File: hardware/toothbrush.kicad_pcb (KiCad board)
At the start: 2 copper layers, 41.5 x 19 mm, 16 parts, among them J2 ISP, J3 MOTOR, J4 BATTERY, Q1 FN337N, SW1 button, U1 ATmega328P-A

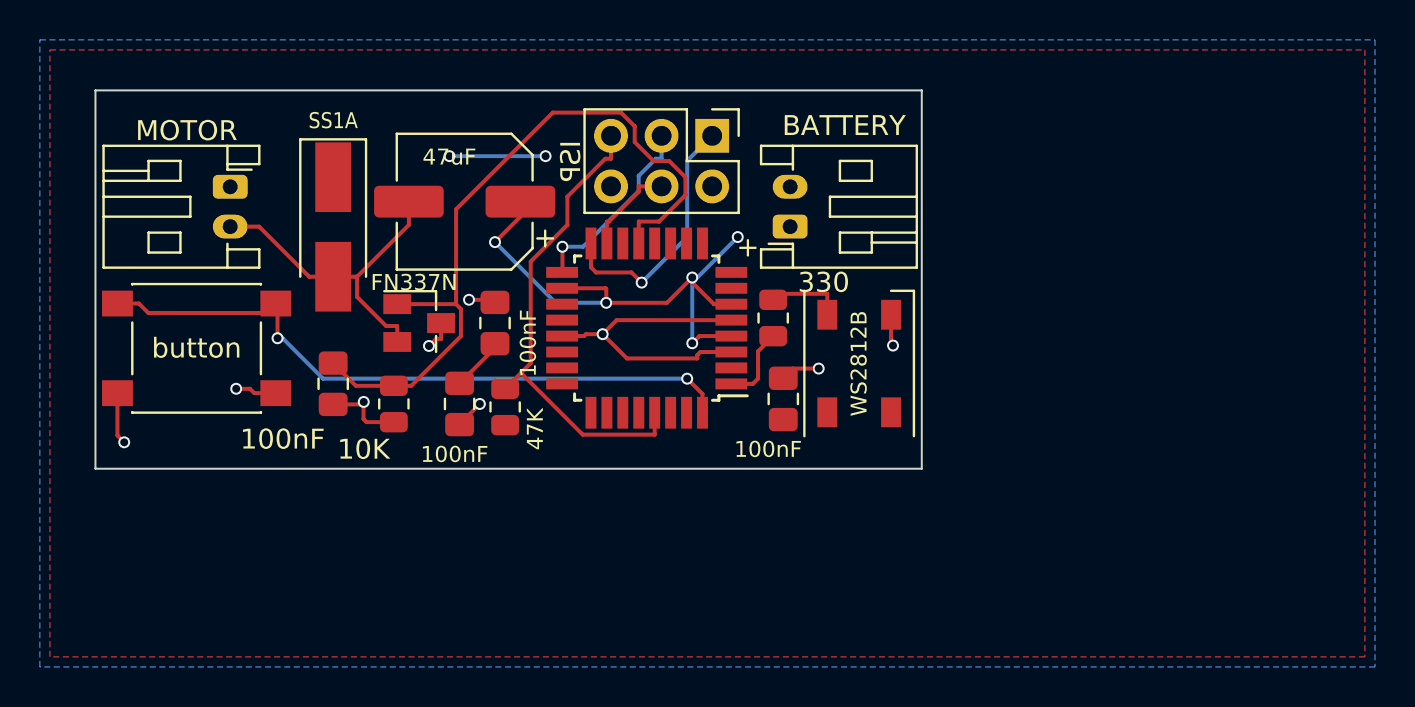
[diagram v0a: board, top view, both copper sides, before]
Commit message: Turn power connector around to be more consistent with other things.
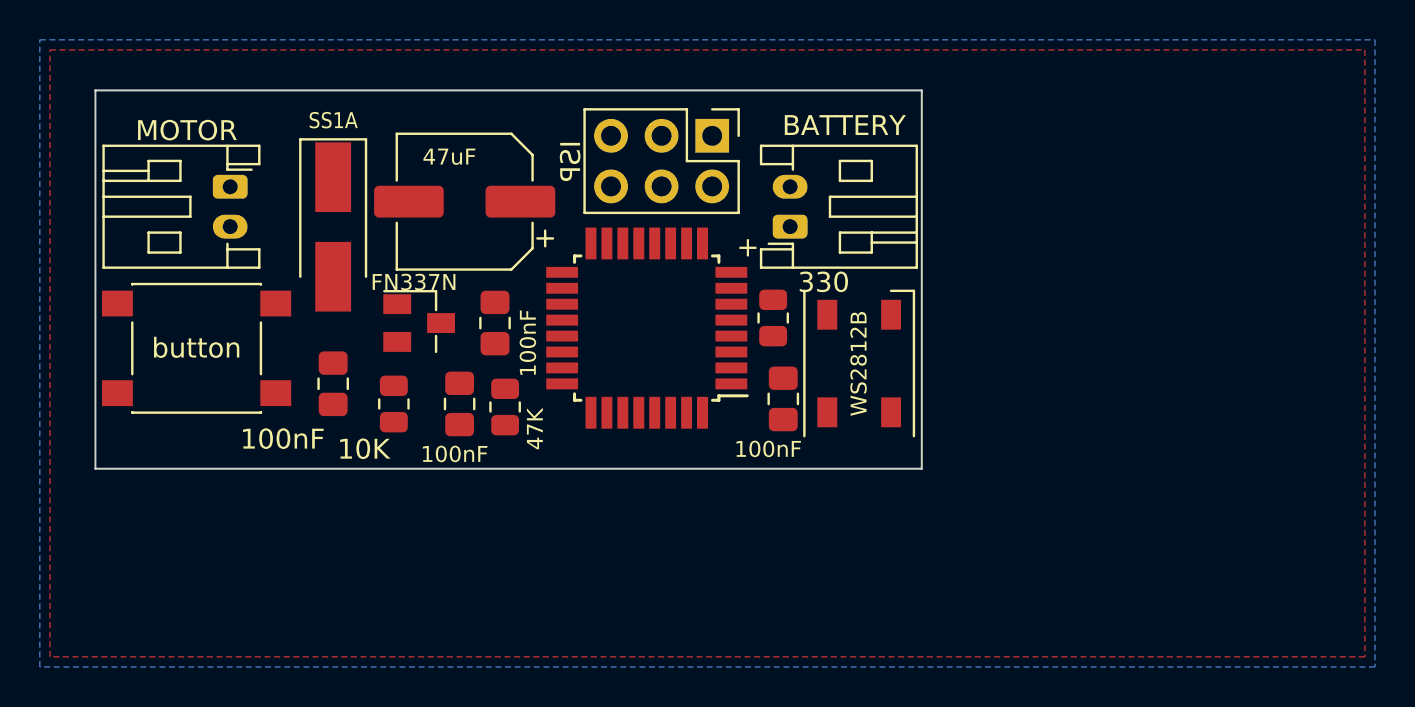
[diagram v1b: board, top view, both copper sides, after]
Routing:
- net /FAN: track 37.6 -> 0.00 mm
- net /VCC: track 35.9 -> 0.00 mm, vias 7 -> 0
- net /BUTTON: track 33.8 -> 0.00 mm, vias 2 -> 0
- net GND: track 32.7 -> 0.00 mm, vias 9 -> 0
- net /RST: track 24.2 -> 0.00 mm
- net Net-(C4-Pad2): track 16.7 -> 0.00 mm
- net /MISO: track 12.9 -> 0.00 mm, vias 1 -> 0
- net /SCK: track 9.70 -> 0.00 mm, vias 1 -> 0
- net /MOSI: track 4.73 -> 0.00 mm
- net /LED: track 3.90 -> 0.00 mm
- net Net-(D2-Pad4): track 3.89 -> 0.00 mm
